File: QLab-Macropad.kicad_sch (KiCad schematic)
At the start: 14 parts, among them SW1 SW_Push, U1 ATmega32U4-A, Y1 16 MHz

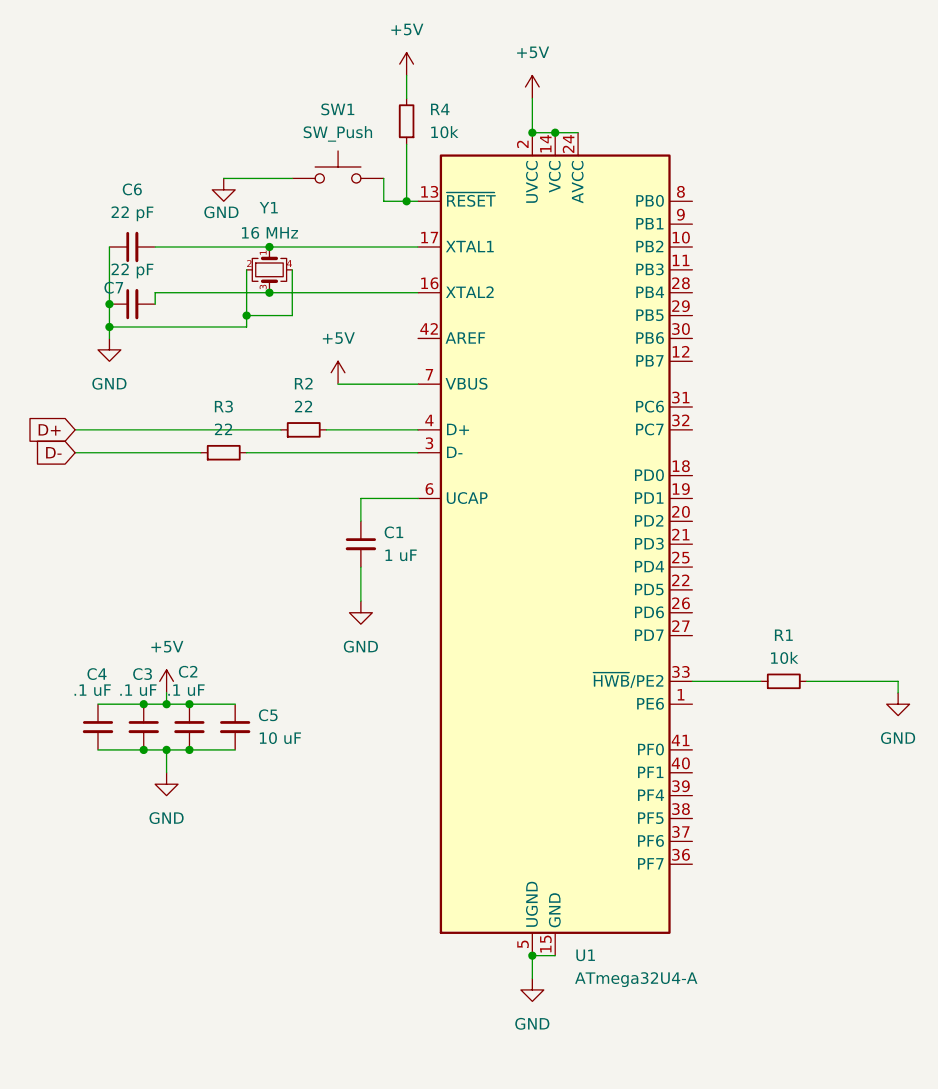
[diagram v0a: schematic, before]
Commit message: Swapped MCUs
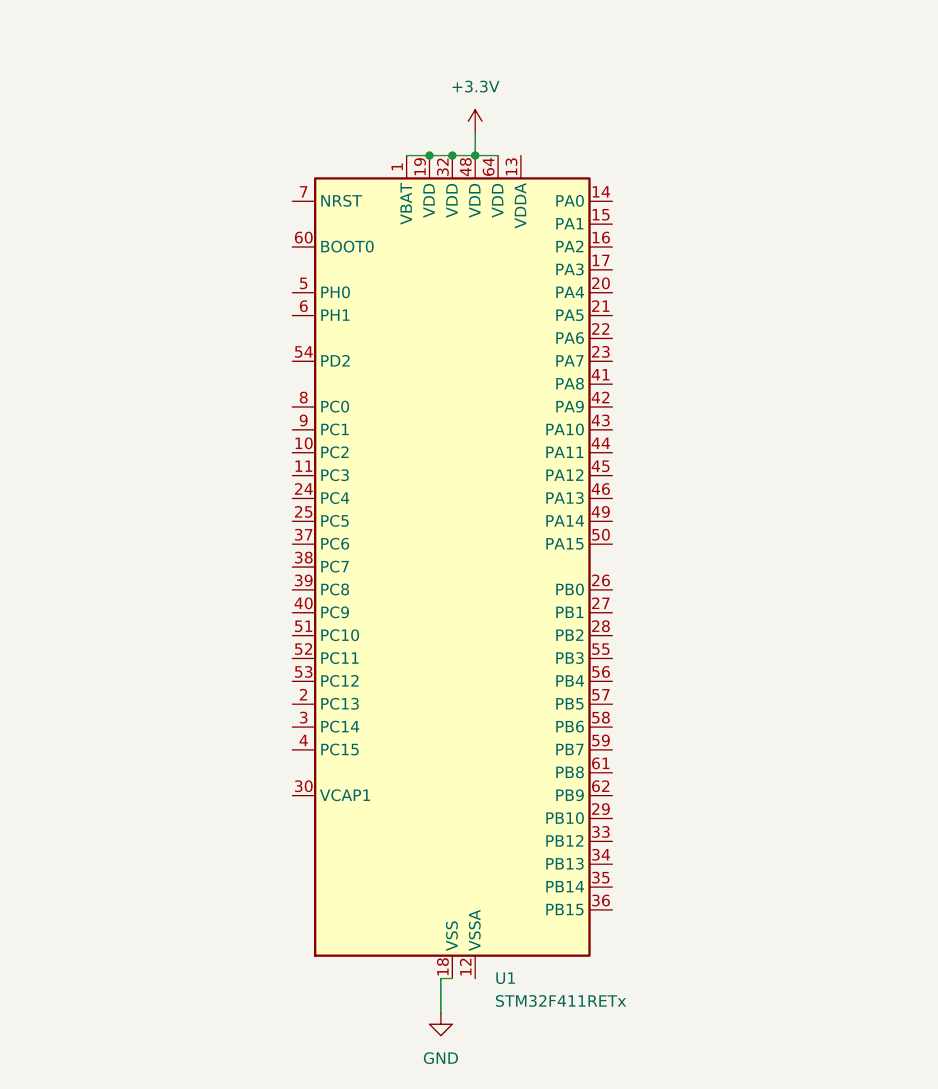
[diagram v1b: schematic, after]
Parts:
- removed C1: 1 uF, symbol Device:C_Small
- removed C2, C3, C4: .1 uF, symbol Device:C_Small
- removed C5: 10 uF, symbol Device:C_Small
- removed C6, C7: 22 pF, symbol Device:C_Small
- removed R1, R4: 10k, symbol Device:R_Small
- removed R2, R3: 22, symbol Device:R_Small
- removed SW1: SW_Push, symbol Switch:SW_Push
- removed U1: ATmega32U4-A, Package_QFP:TQFP-44_10x10mm_P0.8mm, symbol MCU_Microchip_ATmega:ATmega32U4-A
- removed Y1: 16 MHz, symbol Device:Crystal_GND24_Small
- added U1: STM32F411RETx, Package_QFP:LQFP-64_10x10mm_P0.5mm, symbol MCU_ST_STM32F4:STM32F411RETx
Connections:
- net GND: now also U1.18 (VSS), U1.31 (VSS), U1.47 (VSS), U1.63 (VSS)
- new net +3.3V: U1.1 (VBAT), U1.19 (VDD), U1.32 (VDD), U1.48 (VDD), U1.64 (VDD)

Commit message: Worked on decoupling
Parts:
- added C1: 1 μF // 10 nF, symbol Device:C_Small
- added C2, C3: 4.7 uF, symbol Device:C_Small
- added C4-9: 100 nF, symbol Device:C_Small
- added C5, C6, C7, C8, C9: C_Small, symbol Device:C_Small
- added ESR_VCAP: <1, symbol Device:R_Small
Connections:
- net +3.3V: now also C3.1; no longer U1.1 (VBAT), U1.19 (VDD), U1.32 (VDD), U1.48 (VDD), U1.64 (VDD)
- net GND: now also U1.12 (VSSA), C1.2, ESR_VCAP.1
- net at U1.13 (VDDA): now also C9.2
- net at U1.30 (VCAP1): now also C2.2
- new net: C4-9.2, U1.1 (VBAT)
- new net: C5.2, U1.19 (VDD)
- new net: C6.2, U1.32 (VDD)
- new net: C7.2, U1.48 (VDD)
- new net: C8.2, U1.64 (VDD)
- new net: C2.1, ESR_VCAP.2
- new net VDD: C3.2

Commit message: Finished Decoupling
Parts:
- removed C1: 1 μF // 10 nF, symbol Device:C_Small
- removed C4-9: 100 nF, symbol Device:C_Small
- removed C9: C_Small, symbol Device:C_Small
- added C2, C3, C4: 100 nF, symbol Device:C_Small
- C5, C6, C7: value C_Small -> 100 nF
- C8: value C_Small -> 4.7 uF
- renumbered C3 to C1, C2 to VCAP1
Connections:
- net GND: now also C5.1, C6.1, C7.1, C8.1, C2.1, C3.1, C4.1
- net at U1.1 (VBAT): now also C2.2
- net 100 nF: now reaches U1.13 (VDDA)
- net 100 nF: now also C7.2, U1.19 (VDD), C3.2
- net at C5.2: now also U1.48 (VDD); no longer U1.19 (VDD)
- net at U1.32 (VDD): now also C4.2; no longer C6.2
- net at C8.2, U1.64 (VDD): now also C6.2

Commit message: Worked on power supply
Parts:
- removed C1: 4.7 uF, symbol Device:C_Small
- added FB1: FerriteBead_Small, symbol Device:FerriteBead_Small
- added J1: USB4105-GF-A, USB4105-GF-A:GCT_USB4105-GF-A, symbol USB4105-GF-A:USB4105-GF-A
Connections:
- net +3.3V: now also C2.2, C3.2, C4.2, C5.2, C6.2, C7.2, C8.2, U1.1 (VBAT), U1.19 (VDD), U1.32 (VDD), U1.48 (VDD), U1.64 (VDD), FB1.1
- net GND: now also J1.A1_B12 (GND), J1.B1_A12 (GND__1), J1.SH1 (SHELL_GND), J1.SH2 (SHELL_GND__1), J1.SH3 (SHELL_GND__2), J1.SH4 (SHELL_GND__3)
- removed net 100 nF: C3.2, C7.2, U1.13 (VDDA), U1.19 (VDD)
- new net: FB1.2, U1.13 (VDDA)
- new net VBUS Power: J1.A4_B9 (VBUS), J1.B4_A9 (VBUS__1)
- no-connect marks 0 -> 4
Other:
- note added: "Each Vdd should be connected to its own Vss through 100 nF ceramic cap"

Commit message: Finished power for now
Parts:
- added C10, C12: 100 nF, symbol Device:C_Small
- added C11: 680 nF, symbol Device:C_Small
- added C13: 1.5 pF, symbol Device:C_Small
- added C14: 47uF, symbol Device:C_Small
- added C9: 10uF,, symbol Device:C_Small
- added L1: 3.3 uH, symbol Device:L_Small
- added R1: 590 k, symbol Device:R_Small
- added R2: 196 k, symbol Device:R_Small
- added R3: 30.9k, symbol Device:R_Small
- added R4: 10k, symbol Device:R_Small
- added U2: TPS62932, Package_TO_SOT_SMD:SOT-583-8, symbol Regulator_Switching:TPS62932
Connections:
- net GND: now also C10.2, C11.2, C14.2, C9.2, R2.2, R4.2, U2.4 (GND)
- net +3.3V renamed 3.3V 
- net 3.3V : now also C13.1, C14.1, L1.2, R3.1
- net VBUS Power renamed VBUS+
- net VBUS+: now also C10.1, C9.1, R1.1, U2.3 (VIN)
- new net: C13.2, R3.2, R4.1, U2.8 (FB)
- new net: C12.1, U2.6 (BST)
- new net: C12.2, L1.1, U2.5 (SW)
- new net: R1.2, R2.1, U2.2 (EN)
- new net: C11.1, U2.7 (SS)

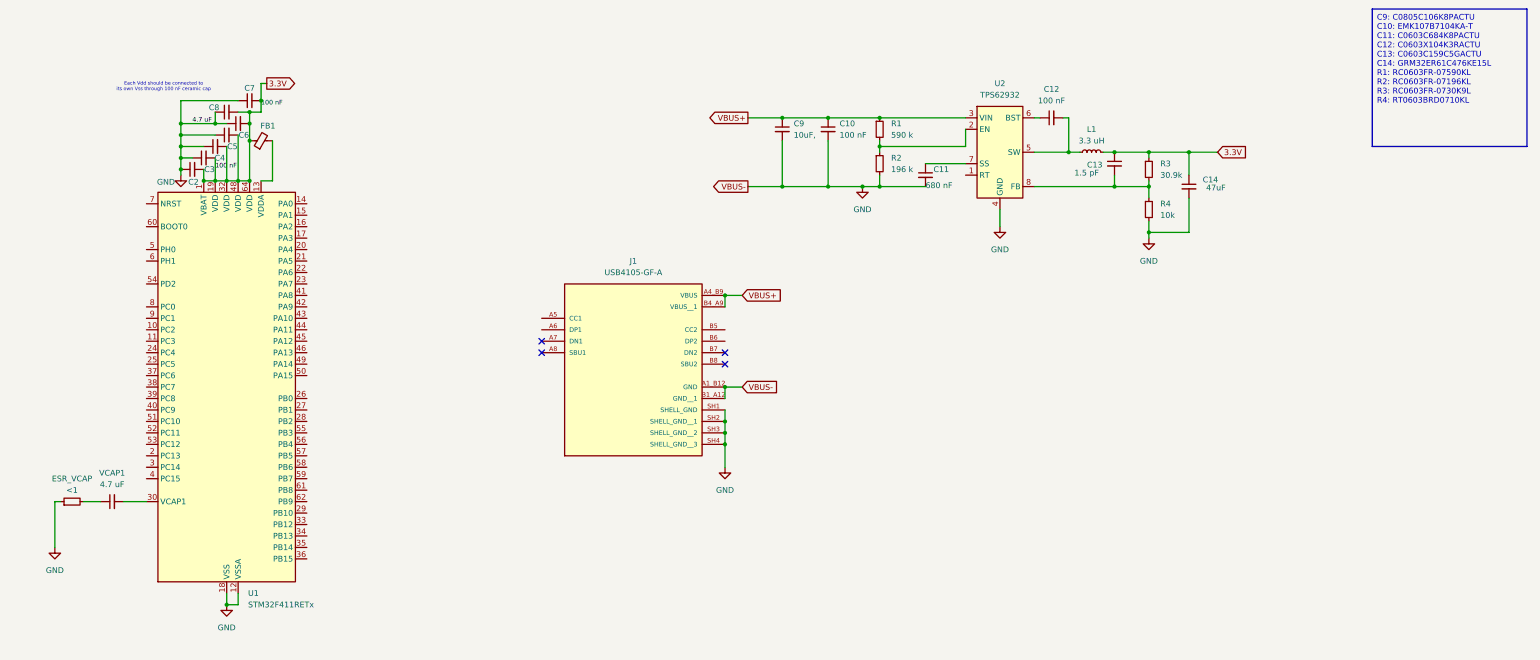
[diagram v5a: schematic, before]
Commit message: Connected power and usb
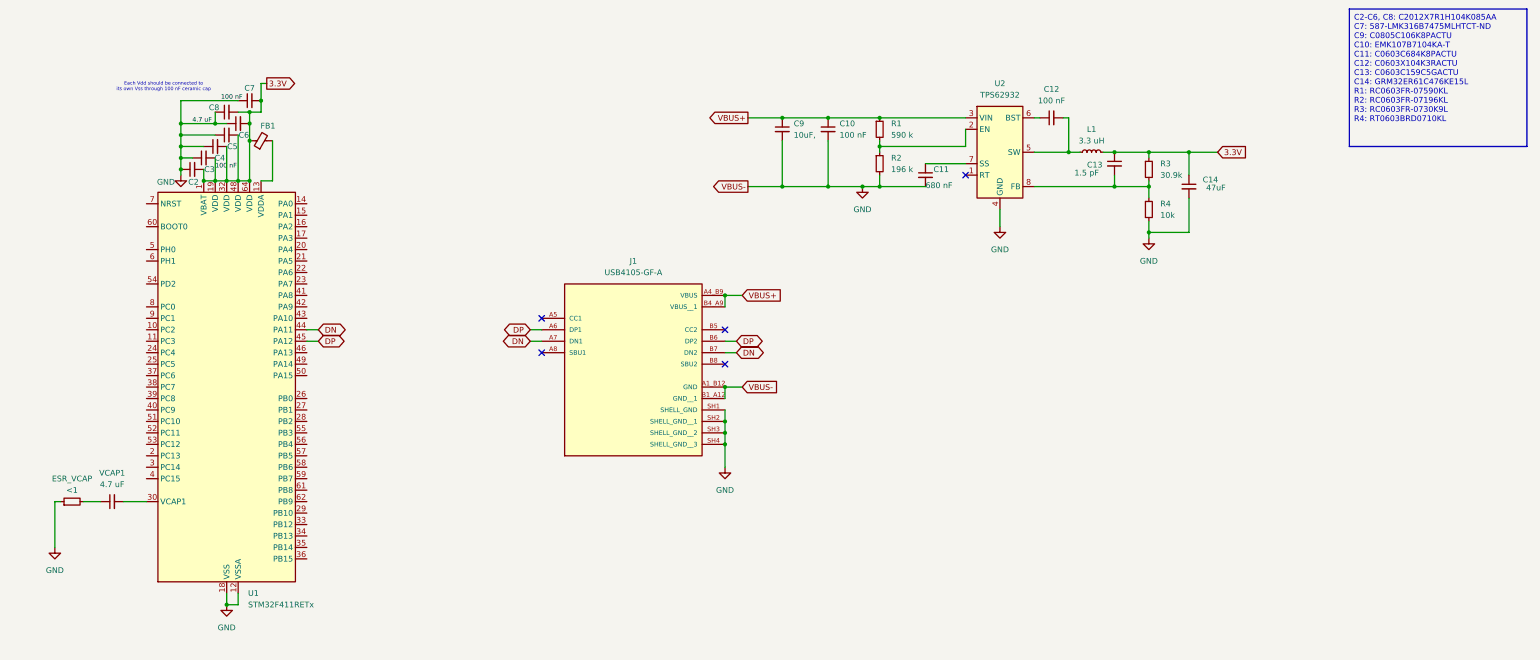
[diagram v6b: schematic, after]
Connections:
- net 3.3V  is gone; now on net GND: C13.1, C14.1, C2.2, C3.2, C4.2, C5.2, C6.2, C7.2, C8.2, FB1.1, L1.2, R3.1, U1.1 (VBAT), U1.19 (VDD), U1.32 (VDD), U1.48 (VDD), U1.64 (VDD)
- net DN: now reaches U1.44 (PA11)
- net DN: now also J1.A7 (DN1), J1.B7 (DN2)
- net DP: now reaches U1.45 (PA12)
- net DP: now also J1.A6 (DP1), J1.B6 (DP2)
- no-connect marks 4 -> 5
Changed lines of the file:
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@@
 	)
 	(no_connect
-		(at 189.23 86.36)
+		(at 189.23 81.28)
 	)
 	(no_connect
-		(at 229.87 88.9)
+		(at 283.21 49.53)
+	)
+	(no_connect
+		(at 229.87 83.82)
 	)
 	(no_connect
@@
 	(wire
 		(pts
+			(xy 137.16 83.82) (xy 139.7 83.82)
+		)
+		(stroke
+			(width 0)
+			(type default)
+		)
+	)
+	(wire
+		(pts
 			(xy 124.46 35.56) (xy 127 35.56)
 		)
@@
 	(wire
 		(pts
+			(xy 127 33.02) (xy 127 35.56)
+		)
+		(stroke
+			(width 0)
+			(type default)
+		)
+	)
+	(wire
+		(pts
 			(xy 116.84 38.1) (xy 109.22 38.1)
 		)
@@
 	(wire
 		(pts
-			(xy 127 35.56) (xy 127 33.02)
-		)
-		(stroke
-			(width 0)
-			(type default)
-		)
-	)
-	(wire
-		(pts
 			(xy 323.85 62.23) (xy 332.74 62.23)
 		)
@@
 	(wire
 		(pts
+			(xy 186.69 86.36) (xy 189.23 86.36)
+		)
+		(stroke
+			(width 0)
+			(type default)
+		)
+	)
+	(wire
+		(pts
 			(xy 332.74 49.53) (xy 332.74 44.45)
 		)
@@
 	(wire
 		(pts
+			(xy 137.16 86.36) (xy 139.7 86.36)
+		)
+		(stroke
+			(width 0)
+			(type default)
+		)
+	)
+	(wire
+		(pts
 			(xy 82.55 121.92) (xy 81.28 121.92)
 		)
@@
 	(wire
 		(pts
+			(xy 186.69 83.82) (xy 189.23 83.82)
+		)
+		(stroke
+			(width 0)
+			(type default)
+		)
+	)
+	(wire
+		(pts
 			(xy 114.3 43.18) (xy 109.22 43.18)
 		)
@@
 	(wire
 		(pts
+			(xy 229.87 86.36) (xy 232.41 86.36)
+		)
+		(stroke
+			(width 0)
+			(type default)
+		)
+	)
+	(wire
+		(pts
 			(xy 121.92 142.24) (xy 121.92 144.78)
 		)
@@
 	(wire
 		(pts
+			(xy 229.87 88.9) (xy 232.41 88.9)
+		)
+		(stroke
+			(width 0)
+			(type default)
+		)
+	)
+	(wire
+		(pts
 			(xy 119.38 43.18) (xy 119.38 50.8)
 		)
@@
 		)
 	)
-	(text_box "C9: C0805C106K8PACTU\nC10: EMK107B7104KA-T\nC11: C0603C684K8PACTU\nC12: C0603X104K3RACTU\nC13: C0603C159C5GACTU\nC14: GRM32ER61C476KE15L\nR1: RC0603FR-07590KL\nR2: RC0603FR-07196KL\nR3: RC0603FR-0730K9L\nR4: RT0603BRD0710KL\n\n"
+	(text_box "C2-C6, C8: C2012X7R1H104K085AA\nC7: 587-LMK316B7475MLHTCT-ND\nC9: C0805C106K8PACTU\nC10: EMK107B7104KA-T\nC11: C0603C684K8PACTU\nC12: C0603X104K3RACTU\nC13: C0603C159C5GACTU\nC14: GRM32ER61C476KE15L\nR1: RC0603FR-07590KL\nR2: RC0603FR-07196KL\nR3: RC0603FR-0730K9L\nR4: RT0603BRD0710KL\n\n"
 		(exclude_from_sim no)
-		(at 373.38 12.7 0)
-		(size 34.29 30.48)
+		(at 368.3 12.7 0)
+		(size 39.37 30.48)
 		(stroke
 			(width 0)
@@
 	)
 	(label "100 nF"
-		(at 127 34.29 0)
+		(at 118.11 33.02 0)
 		(fields_autoplaced yes)
 		(effects
@@
 			)
 			(justify left bottom)
+		)
+	)
+	(global_label "DP"
+		(shape bidirectional)
+		(at 186.69 83.82 180)
+		(fields_autoplaced yes)
+		(effects
+			(font
+				(size 1.27 1.27)
+			)
+			(justify right)
+		)
+		(property "Intersheetrefs" "${INTERSHEET_REFS}"
+			(at 180.0535 83.82 0)
+			(effects
+				(font
+					(size 1.27 1.27)
+				)
+				(justify right)
+				(hide yes)
+			)
 		)
 	)
@@
 		)
 	)
+	(global_label "DP"
+		(shape bidirectional)
+		(at 232.41 86.36 0)
+		(fields_autoplaced yes)
+		(effects
+			(font
+				(size 1.27 1.27)
+			)
+			(justify left)
+		)
+		(property "Intersheetrefs" "${INTERSHEET_REFS}"
+			(at 239.0465 86.36 0)
+			(effects
+				(font
+					(size 1.27 1.27)
+				)
+				(justify left)
+				(hide yes)
+			)
+		)
+	)
 	(global_label "3.3V "
 		(shape input)
@@
 		)
 	)
+	(global_label "DN"
+		(shape bidirectional)
+		(at 232.41 88.9 0)
+		(fields_autoplaced yes)
+		(effects
+			(font
+				(size 1.27 1.27)
+			)
+			(justify left)
+		)
+		(property "Intersheetrefs" "${INTERSHEET_REFS}"
+			(at 239.107 88.9 0)
+			(effects
+				(font
+					(size 1.27 1.27)
+				)
+				(justify left)
+				(hide yes)
+			)
+		)
+	)
+	(global_label "DN"
+		(shape bidirectional)
+		(at 186.69 86.36 180)
+		(fields_autoplaced yes)
+		(effects
+			(font
+				(size 1.27 1.27)
+			)
+			(justify right)
+		)
+		(property "Intersheetrefs" "${INTERSHEET_REFS}"
+			(at 179.993 86.36 0)
+			(effects
+				(font
+					(size 1.27 1.27)
+				)
+				(justify right)
+				(hide yes)
+			)
+		)
+	)
+	(global_label "DP"
+		(shape bidirectional)
+		(at 139.7 86.36 0)
+		(fields_autoplaced yes)
+		(effects
+			(font
+				(size 1.27 1.27)
+			)
+			(justify left)
+		)
+		(property "Intersheetrefs" "${INTERSHEET_REFS}"
+			(at 146.3365 86.36 0)
+			(effects
+				(font
+					(size 1.27 1.27)
+				)
+				(justify left)
+				(hide yes)
+			)
+		)
+	)
 	(global_label "VBUS+"
 		(shape output)
@@
 				(hide yes)
 			)
+		)
+	)
+	(global_label "DN"
+		(shape bidirectional)
+		(at 139.7 83.82 0)
+		(fields_autoplaced yes)
+		(effects
+			(font
+				(size 1.27 1.27)
+			)
+			(justify left)
+		)
+		(property "Intersheetrefs" "${INTERSHEET_REFS}"
+			(at 146.397 83.82 0)
+			(effects
+				(font
+					(size 1.27 1.27)
+				)
+				(justify left)
+				(hide yes)
+			)
